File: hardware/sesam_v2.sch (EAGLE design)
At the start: 13 parts, among them IC1 337T

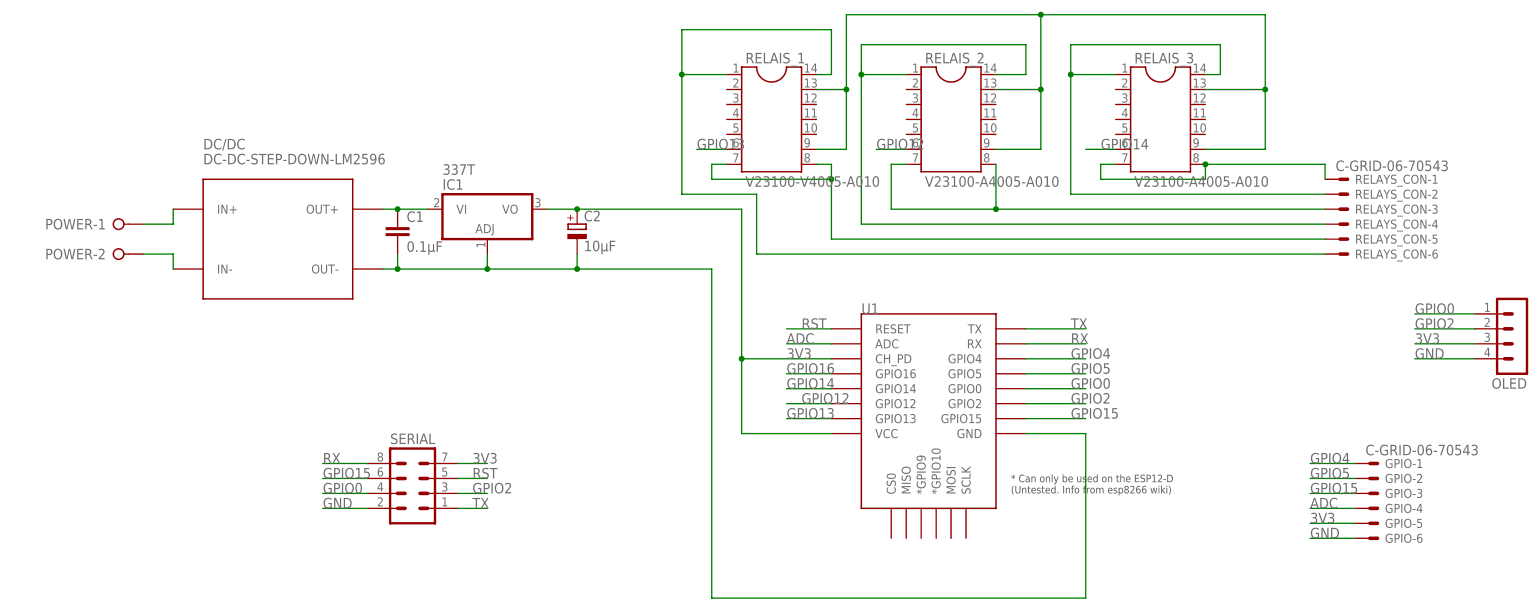
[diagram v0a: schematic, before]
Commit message: switched to the correct regulator
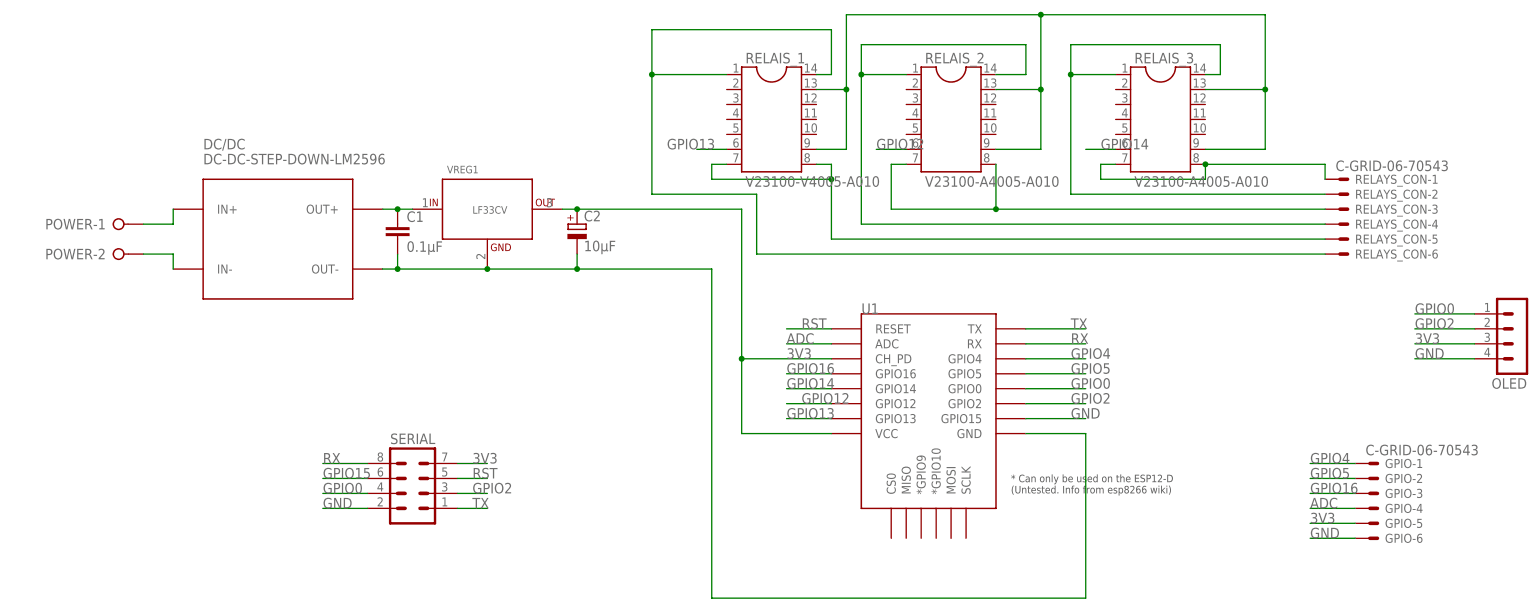
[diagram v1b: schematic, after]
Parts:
- removed IC1: 337T, linear:337T
- added VREG1: LF33CV, mp_vreg:LF33CV
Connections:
- net 3V3: now also VREG1.OUT; no longer IC1.VO
- net GND: now also U1.GPIO15, VREG1.GND; no longer IC1.ADJ
- net GPIO15: no longer GPIO-3.S, U1.GPIO15
- net GPIO16: now also GPIO-3.S
- net POWER: now also VREG1.IN; no longer IC1.VI
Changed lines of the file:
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@@
 <part name="POWER" library="con-wago-508" deviceset="W237-02P" device=""/>
 <part name="GPIO" library="con-molex" deviceset="C-GRID-06" device="-70543"/>
-<part name="IC1" library="linear" deviceset="*337" device="T"/>
 <part name="C1" library="rcl" deviceset="C-EU" device="C0805" value="0.1µF"/>
 <part name="C2" library="rcl" deviceset="CPOL-EU" device="E2-5" value="10µF"/>
+<part name="VREG1" library="mp_vreg" deviceset="LF33CV" device=""/>
 </parts>
 <sheets>
@@
 <instance part="GPIO" gate="-5" x="175.26" y="20.32"/>
 <instance part="GPIO" gate="-6" x="175.26" y="17.78"/>
-<instance part="IC1" gate="A1" x="25.4" y="73.66" rot="MR180"/>
 <instance part="C1" gate="G$1" x="10.16" y="71.12"/>
 <instance part="C2" gate="G$1" x="40.64" y="71.12"/>
+<instance part="VREG1" gate="G$1" x="25.4" y="73.66"/>
 </instances>
 <busses>
@@
 <wire x1="7.62" y1="63.5" x2="10.16" y2="63.5" width="0.1524" layer="91"/>
 <wire x1="10.16" y1="63.5" x2="10.16" y2="66.04" width="0.1524" layer="91"/>
-<pinref part="IC1" gate="A1" pin="ADJ"/>
 <wire x1="10.16" y1="63.5" x2="25.4" y2="63.5" width="0.1524" layer="91"/>
-<wire x1="25.4" y1="63.5" x2="25.4" y2="66.04" width="0.1524" layer="91"/>
 <junction x="10.16" y="63.5"/>
 <pinref part="C2" gate="G$1" pin="-"/>
@@
 <pinref part="U1" gate="G$1" pin="GND"/>
 <wire x1="127" y1="35.56" x2="116.84" y2="35.56" width="0.1524" layer="91"/>
+<pinref part="VREG1" gate="G$1" pin="GND"/>
 </segment>
 <segment>
@@
 <label x="-2.54" y="22.86" size="1.778" layer="95"/>
 </segment>
+<segment>
+<pinref part="U1" gate="G$1" pin="GPIO15"/>
+<wire x1="116.84" y1="38.1" x2="127" y2="38.1" width="0.1524" layer="91"/>
+<label x="124.46" y="38.1" size="1.778" layer="95"/>
+</segment>
 </net>
 <net name="N$4" class="0">
@@
 <pinref part="C1" gate="G$1" pin="1"/>
 <wire x1="7.62" y1="73.66" x2="10.16" y2="73.66" width="0.1524" layer="91"/>
-<pinref part="IC1" gate="A1" pin="VI"/>
-<wire x1="10.16" y1="73.66" x2="15.24" y2="73.66" width="0.1524" layer="91"/>
+<wire x1="10.16" y1="73.66" x2="12.7" y2="73.66" width="0.1524" layer="91"/>
 <junction x="10.16" y="73.66"/>
+<pinref part="VREG1" gate="G$1" pin="IN"/>
 </segment>
 </net>
@@
 <junction x="68.58" y="48.26"/>
 <label x="76.2" y="48.26" size="1.778" layer="95"/>
-<pinref part="IC1" gate="A1" pin="VO"/>
-<wire x1="40.64" y1="73.66" x2="35.56" y2="73.66" width="0.1524" layer="91"/>
+<wire x1="40.64" y1="73.66" x2="38.1" y2="73.66" width="0.1524" layer="91"/>
 <junction x="40.64" y="73.66"/>
+<pinref part="VREG1" gate="G$1" pin="OUT"/>
 </segment>
 <segment>
@@
 <wire x1="167.64" y1="66.04" x2="71.12" y2="66.04" width="0.1524" layer="91"/>
 <wire x1="71.12" y1="66.04" x2="71.12" y2="76.2" width="0.1524" layer="91"/>
-<wire x1="71.12" y1="76.2" x2="58.42" y2="76.2" width="0.1524" layer="91"/>
-<wire x1="58.42" y1="76.2" x2="58.42" y2="96.52" width="0.1524" layer="91"/>
-<wire x1="58.42" y1="96.52" x2="58.42" y2="104.14" width="0.1524" layer="91"/>
-<wire x1="58.42" y1="104.14" x2="83.82" y2="104.14" width="0.1524" layer="91"/>
+<wire x1="71.12" y1="76.2" x2="53.34" y2="76.2" width="0.1524" layer="91"/>
+<wire x1="53.34" y1="76.2" x2="53.34" y2="96.52" width="0.1524" layer="91"/>
+<wire x1="53.34" y1="96.52" x2="53.34" y2="104.14" width="0.1524" layer="91"/>
+<wire x1="53.34" y1="104.14" x2="83.82" y2="104.14" width="0.1524" layer="91"/>
 <wire x1="83.82" y1="104.14" x2="83.82" y2="96.52" width="0.1524" layer="91"/>
 <pinref part="RELAIS_1" gate="G$1" pin="14"/>
 <wire x1="83.82" y1="96.52" x2="81.28" y2="96.52" width="0.1524" layer="91"/>
 <pinref part="RELAIS_1" gate="G$1" pin="1"/>
-<wire x1="66.04" y1="96.52" x2="58.42" y2="96.52" width="0.1524" layer="91"/>
-<junction x="58.42" y="96.52"/>
+<wire x1="66.04" y1="96.52" x2="53.34" y2="96.52" width="0.1524" layer="91"/>
+<junction x="53.34" y="96.52"/>
 </segment>
 </net>
@@
 <label x="76.2" y="45.72" size="1.778" layer="95"/>
 </segment>
+<segment>
+<pinref part="GPIO" gate="-3" pin="S"/>
+<wire x1="172.72" y1="25.4" x2="165.1" y2="25.4" width="0.1524" layer="91"/>
+<label x="165.1" y="25.4" size="1.778" layer="95"/>
+</segment>
 </net>
 <net name="GPIO14" class="0">
@@
 <pinref part="RELAIS_1" gate="G$1" pin="6"/>
 <wire x1="66.04" y1="83.82" x2="60.96" y2="83.82" width="0.1524" layer="91"/>
-<label x="60.96" y="83.82" size="1.778" layer="95"/>
+<label x="55.88" y="83.82" size="1.778" layer="95"/>
 </segment>
 </net>
@@
 <net name="GPIO15" class="0">
 <segment>
-<pinref part="U1" gate="G$1" pin="GPIO15"/>
-<wire x1="116.84" y1="38.1" x2="127" y2="38.1" width="0.1524" layer="91"/>
-<label x="124.46" y="38.1" size="1.778" layer="95"/>
-</segment>
-<segment>
 <pinref part="SERIAL" gate="G$1" pin="6"/>
 <wire x1="5.08" y1="27.94" x2="-2.54" y2="27.94" width="0.1524" layer="91"/>
 <label x="-2.54" y="27.94" size="1.778" layer="95"/>
 </segment>
-<segment>
-<pinref part="GPIO" gate="-3" pin="S"/>
-<wire x1="172.72" y1="25.4" x2="165.1" y2="25.4" width="0.1524" layer="91"/>
-<label x="165.1" y="25.4" size="1.778" layer="95"/>
-</segment>
-</net>
+</net>

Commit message: minor tweaks of the board and change of display text size
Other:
- moved on the sheet: C1, C2, DC/DC, POWER-1, POWER-2, VREG1
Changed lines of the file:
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@@
 <instances>
 <instance part="U1" gate="G$1" x="101.6" y="45.72"/>
-<instance part="DC/DC" gate="G$1" x="-10.16" y="68.58"/>
+<instance part="DC/DC" gate="G$1" x="-12.7" y="53.34"/>
 <instance part="RELAYS_CON" gate="-1" x="170.18" y="78.74"/>
 <instance part="RELAYS_CON" gate="-2" x="170.18" y="76.2"/>
@@
 <instance part="SERIAL" gate="G$1" x="12.7" y="27.94"/>
 <instance part="OLED" gate="1" x="200.66" y="50.8" rot="R180"/>
-<instance part="POWER" gate="-1" x="-38.1" y="71.12"/>
-<instance part="POWER" gate="-2" x="-38.1" y="66.04"/>
+<instance part="POWER" gate="-1" x="-40.64" y="55.88"/>
+<instance part="POWER" gate="-2" x="-40.64" y="50.8"/>
 <instance part="GPIO" gate="-1" x="175.26" y="30.48"/>
 <instance part="GPIO" gate="-2" x="175.26" y="27.94"/>
@@
 <instance part="GPIO" gate="-5" x="175.26" y="20.32"/>
 <instance part="GPIO" gate="-6" x="175.26" y="17.78"/>
-<instance part="C1" gate="G$1" x="10.16" y="71.12"/>
-<instance part="C2" gate="G$1" x="40.64" y="71.12"/>
-<instance part="VREG1" gate="G$1" x="25.4" y="73.66"/>
+<instance part="C1" gate="G$1" x="7.62" y="55.88"/>
+<instance part="C2" gate="G$1" x="38.1" y="55.88"/>
+<instance part="VREG1" gate="G$1" x="22.86" y="58.42"/>
 </instances>
 <busses>
@@
 <pinref part="POWER" gate="-2" pin="KL"/>
 <pinref part="DC/DC" gate="G$1" pin="IN-"/>
-<wire x1="-33.02" y1="66.04" x2="-27.94" y2="66.04" width="0.1524" layer="91"/>
-<wire x1="-27.94" y1="66.04" x2="-27.94" y2="63.5" width="0.1524" layer="91"/>
+<wire x1="-35.56" y1="50.8" x2="-30.48" y2="50.8" width="0.1524" layer="91"/>
+<wire x1="-30.48" y1="50.8" x2="-30.48" y2="48.26" width="0.1524" layer="91"/>
 </segment>
 <segment>
 <pinref part="DC/DC" gate="G$1" pin="OUT-"/>
 <pinref part="C1" gate="G$1" pin="2"/>
-<wire x1="7.62" y1="63.5" x2="10.16" y2="63.5" width="0.1524" layer="91"/>
-<wire x1="10.16" y1="63.5" x2="10.16" y2="66.04" width="0.1524" layer="91"/>
-<wire x1="10.16" y1="63.5" x2="25.4" y2="63.5" width="0.1524" layer="91"/>
-<junction x="10.16" y="63.5"/>
+<wire x1="5.08" y1="48.26" x2="7.62" y2="48.26" width="0.1524" layer="91"/>
+<wire x1="7.62" y1="48.26" x2="7.62" y2="50.8" width="0.1524" layer="91"/>
+<wire x1="7.62" y1="48.26" x2="22.86" y2="48.26" width="0.1524" layer="91"/>
+<junction x="7.62" y="48.26"/>
 <pinref part="C2" gate="G$1" pin="-"/>
-<wire x1="25.4" y1="63.5" x2="40.64" y2="63.5" width="0.1524" layer="91"/>
-<wire x1="40.64" y1="63.5" x2="40.64" y2="66.04" width="0.1524" layer="91"/>
-<junction x="25.4" y="63.5"/>
-<wire x1="40.64" y1="63.5" x2="63.5" y2="63.5" width="0.1524" layer="91"/>
-<wire x1="63.5" y1="63.5" x2="63.5" y2="7.62" width="0.1524" layer="91"/>
-<junction x="40.64" y="63.5"/>
+<wire x1="22.86" y1="48.26" x2="38.1" y2="48.26" width="0.1524" layer="91"/>
+<wire x1="38.1" y1="48.26" x2="38.1" y2="50.8" width="0.1524" layer="91"/>
+<junction x="22.86" y="48.26"/>
+<wire x1="38.1" y1="48.26" x2="63.5" y2="48.26" width="0.1524" layer="91"/>
+<wire x1="63.5" y1="48.26" x2="63.5" y2="7.62" width="0.1524" layer="91"/>
+<junction x="38.1" y="48.26"/>
 <wire x1="63.5" y1="7.62" x2="127" y2="7.62" width="0.1524" layer="91"/>
 <wire x1="127" y1="7.62" x2="127" y2="35.56" width="0.1524" layer="91"/>
@@
 <wire x1="127" y1="35.56" x2="116.84" y2="35.56" width="0.1524" layer="91"/>
 <pinref part="VREG1" gate="G$1" pin="GND"/>
+<label x="50.8" y="50.8" size="1.778" layer="95"/>
 </segment>
 <segment>
@@
 <pinref part="POWER" gate="-1" pin="KL"/>
 <pinref part="DC/DC" gate="G$1" pin="IN+"/>
-<wire x1="-33.02" y1="71.12" x2="-27.94" y2="71.12" width="0.1524" layer="91"/>
-<wire x1="-27.94" y1="71.12" x2="-27.94" y2="73.66" width="0.1524" layer="91"/>
+<wire x1="-35.56" y1="55.88" x2="-30.48" y2="55.88" width="0.1524" layer="91"/>
+<wire x1="-30.48" y1="55.88" x2="-30.48" y2="58.42" width="0.1524" layer="91"/>
 </segment>
 </net>
@@
 <pinref part="DC/DC" gate="G$1" pin="OUT+"/>
 <pinref part="C1" gate="G$1" pin="1"/>
-<wire x1="7.62" y1="73.66" x2="10.16" y2="73.66" width="0.1524" layer="91"/>
-<wire x1="10.16" y1="73.66" x2="12.7" y2="73.66" width="0.1524" layer="91"/>
-<junction x="10.16" y="73.66"/>
+<wire x1="5.08" y1="58.42" x2="7.62" y2="58.42" width="0.1524" layer="91"/>
+<wire x1="7.62" y1="58.42" x2="10.16" y2="58.42" width="0.1524" layer="91"/>
+<junction x="7.62" y="58.42"/>
 <pinref part="VREG1" gate="G$1" pin="IN"/>
 </segment>
@@
 <segment>
 <pinref part="C2" gate="G$1" pin="+"/>
-<wire x1="40.64" y1="73.66" x2="68.58" y2="73.66" width="0.1524" layer="91"/>
-<wire x1="68.58" y1="73.66" x2="68.58" y2="48.26" width="0.1524" layer="91"/>
+<wire x1="38.1" y1="58.42" x2="68.58" y2="58.42" width="0.1524" layer="91"/>
+<wire x1="68.58" y1="58.42" x2="68.58" y2="48.26" width="0.1524" layer="91"/>
 <pinref part="U1" gate="G$1" pin="VCC"/>
 <wire x1="68.58" y1="48.26" x2="68.58" y2="35.56" width="0.1524" layer="91"/>
@@
 <junction x="68.58" y="48.26"/>
 <label x="76.2" y="48.26" size="1.778" layer="95"/>
-<wire x1="40.64" y1="73.66" x2="38.1" y2="73.66" width="0.1524" layer="91"/>
-<junction x="40.64" y="73.66"/>
+<wire x1="38.1" y1="58.42" x2="35.56" y2="58.42" width="0.1524" layer="91"/>
+<junction x="38.1" y="58.42"/>
 <pinref part="VREG1" gate="G$1" pin="OUT"/>
+<label x="50.8" y="60.96" size="1.778" layer="95"/>
 </segment>
 <segment>
